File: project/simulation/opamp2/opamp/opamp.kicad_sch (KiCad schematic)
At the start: 10 parts, among them U1 OPAMP, U2 OPAMP

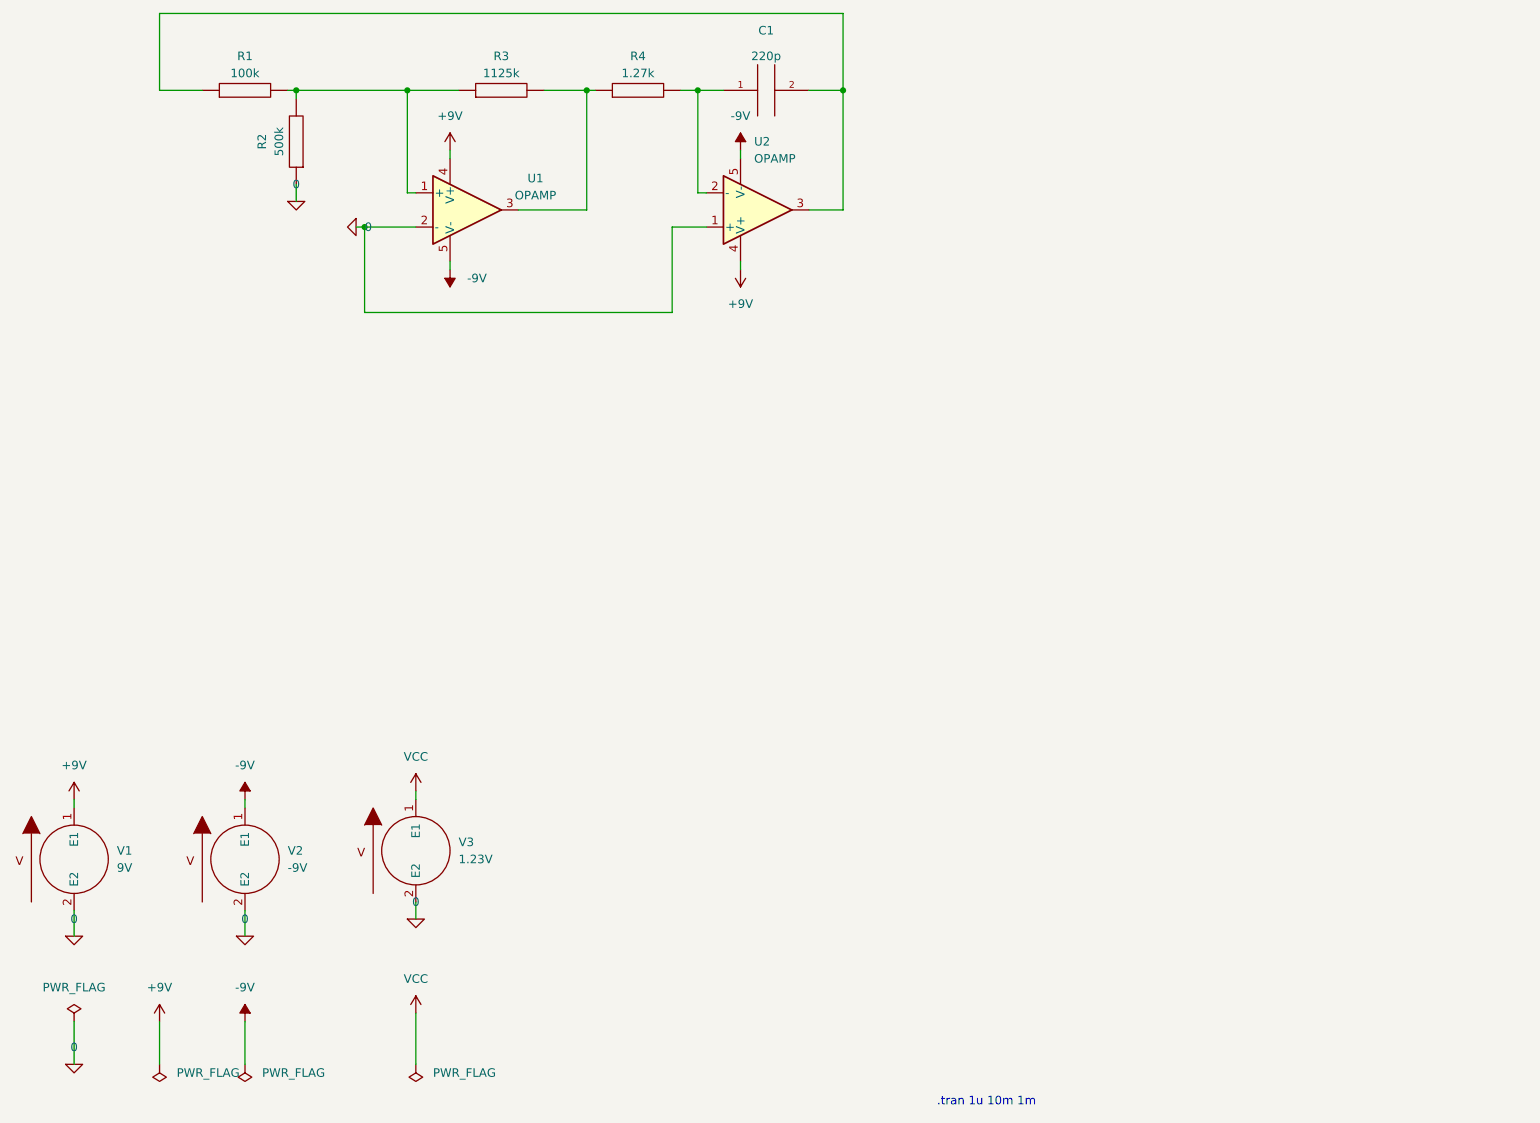
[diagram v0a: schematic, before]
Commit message: I simulated different opamp circuits, I'm facing with problems on peaks when I increase frequency, I think I should change opamp's spice mode, if I overcome the issue, then I'll start to simulate transistor TWG
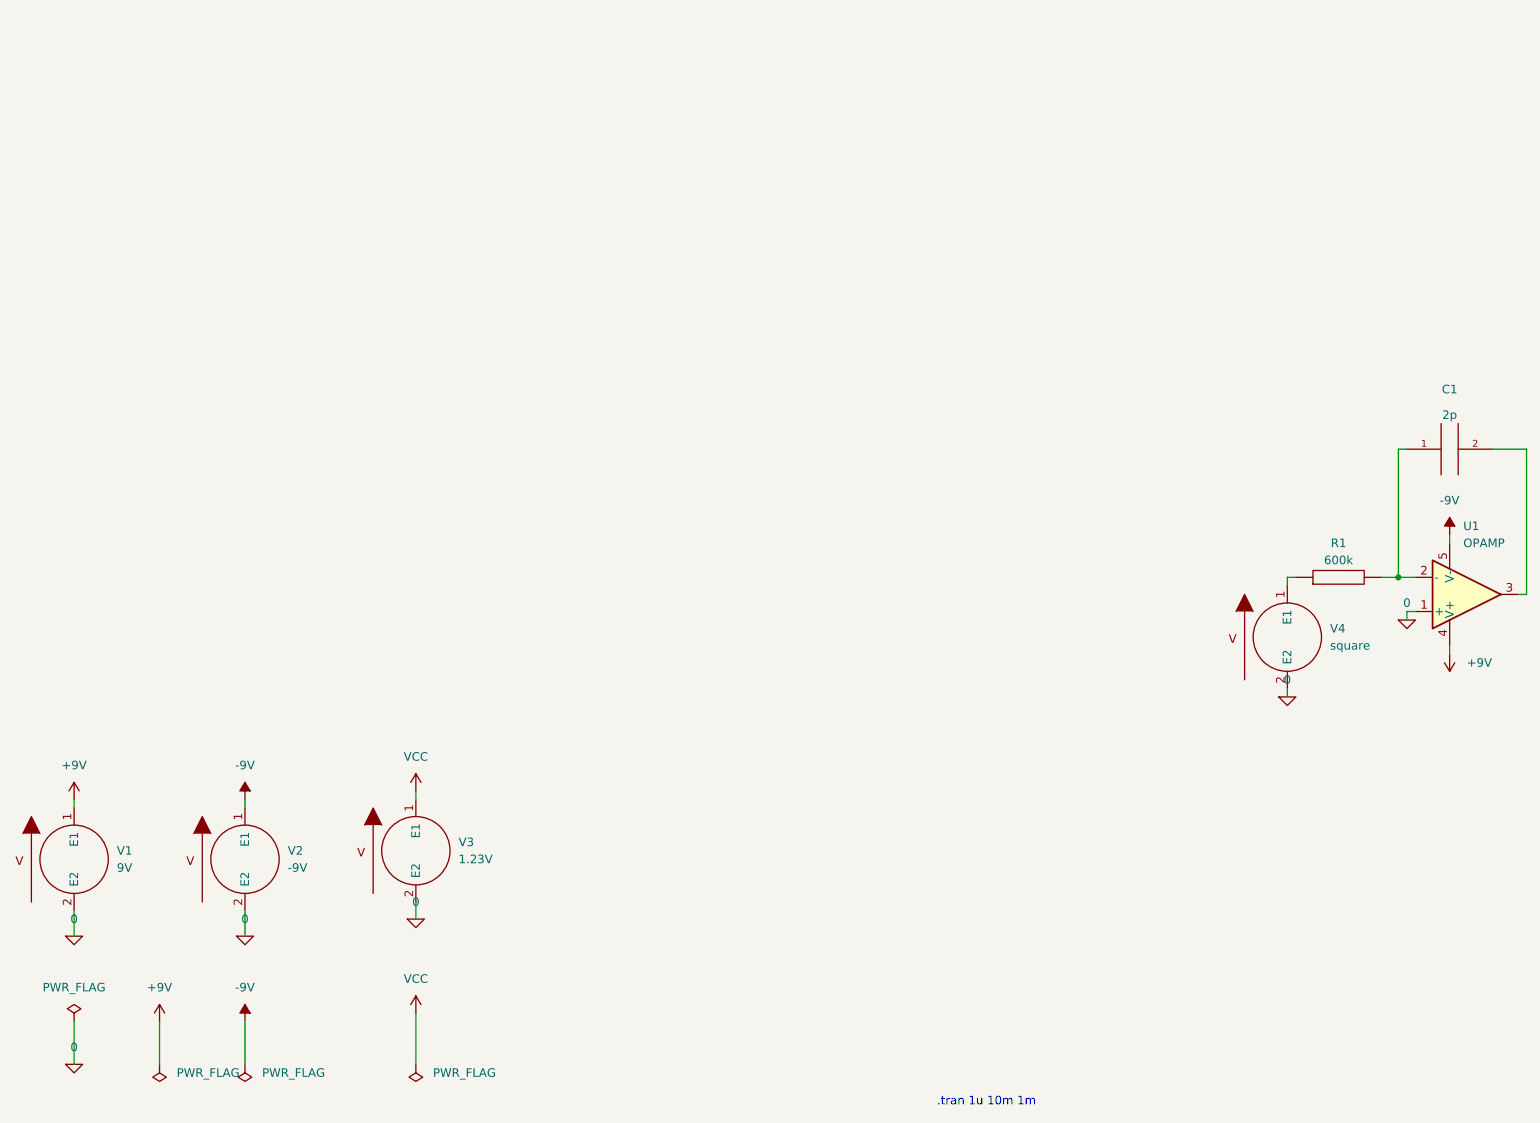
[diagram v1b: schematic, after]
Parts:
- removed R2, R3, R4: 1, symbol pspice:R
- removed U2: OPAMP, symbol pspice:OPAMP
- added V4: square, symbol pspice:VSOURCE
- C1: Spice_Model 220p -> 2p
- R1: Spice_Model 100k -> 600k
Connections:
- net 0: now also U1.1 (+), V4.2 (E2); no longer U1.2 (-)
- net at R1.2: now also C1.1, U1.2 (-); no longer U1.1 (+)
- net at U1.3: now also C1.2
- net at R1.1: now also V4.1 (E1); no longer C1.2
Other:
- moved on the sheet: C1
